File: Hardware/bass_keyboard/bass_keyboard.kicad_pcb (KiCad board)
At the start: 2 copper layers, 291.3 x 154.8 mm, 188 parts, among them J1 Conn_02x17_Top_Bottom

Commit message: Redo traces on bass keyboard
Completely started over on the traces, decided that the automatic routing was whack. Much happier with the new layout, increased orderliness and legibility, less prone to manufacturing error due to via clearance. Also adjusted speaker connection to better fit 16 AWG speaker wire.
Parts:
- LS1: footprint Connector_Wire:SolderWire-2sqmm_1x02_P7.8mm_D2mm_OD3.9mm -> Connector_Wire:SolderWire-1sqmm_1x02_P5.4mm_D1.4mm_OD2.7mm
- moved D79 0.67 mm to (61.1, 206.5)
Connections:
- J1 pad 11: unconnected-(J1-Pin_11-Pad11) -> ROW6
- J1 pad 34: ROW6 -> unconnected-(J1-Pin_34-Pad34)
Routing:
- net (no net): track 110.5 -> 0.00 mm
- net ROW2: track 449.9 -> 376.0 mm, vias 2 -> 0
- net ROW0: track 488.0 -> 426.7 mm
- net ROW5: track 374.3 -> 316.5 mm, vias 4 -> 0
- net ROW3: track 411.6 -> 365.3 mm, vias 2 -> 0
- net ROW4: track 301.9 -> 338.9 mm, vias 4 -> 0
- net COL12: track 333.5 -> 369.8 mm
- net Net-(D95_Dom7-K): track 236.6 -> 257.5 mm
- net COL1: track 159.7 -> 179.4 mm
- net COL8: track 273.4 -> 290.1 mm, vias 2 -> 0
- net COL9: track 291.5 -> 307.8 mm, vias 2 -> 0
- net Net-(D93_Dim1-K): track 229.2 -> 245.0 mm
- net COL2: track 176.6 -> 192.2 mm
- net Net-(J1-Pin_19): track 331.0 -> 316.0 mm
- net COL11: track 337.6 -> 352.4 mm
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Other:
- board text added: "Synharmonium Bass Keyboard Protoyping Master rev 0.2"
- board text removed: "Synharmonium Bass Keyboard Protoyping Master rev 0.1"

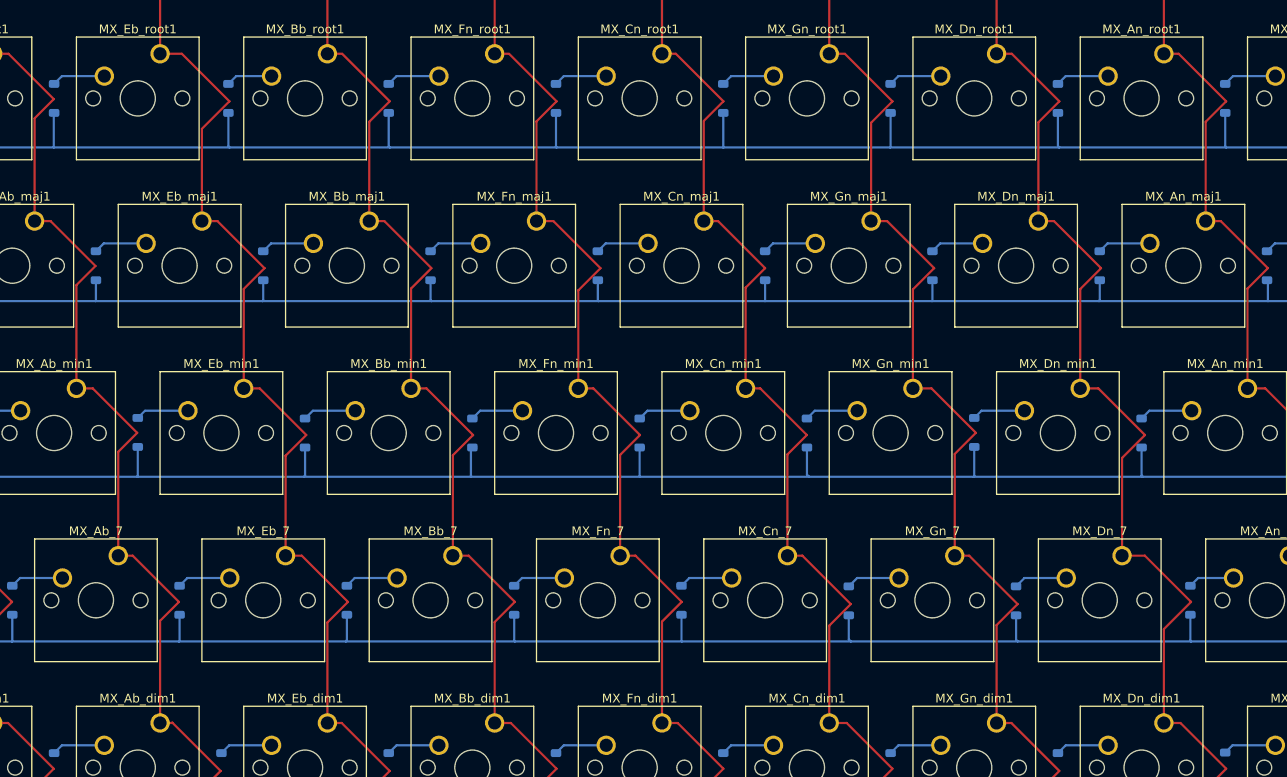
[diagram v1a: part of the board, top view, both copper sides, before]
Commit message: Added Website folder
A custom web page will be hosted through github, and the source files will be stored here.
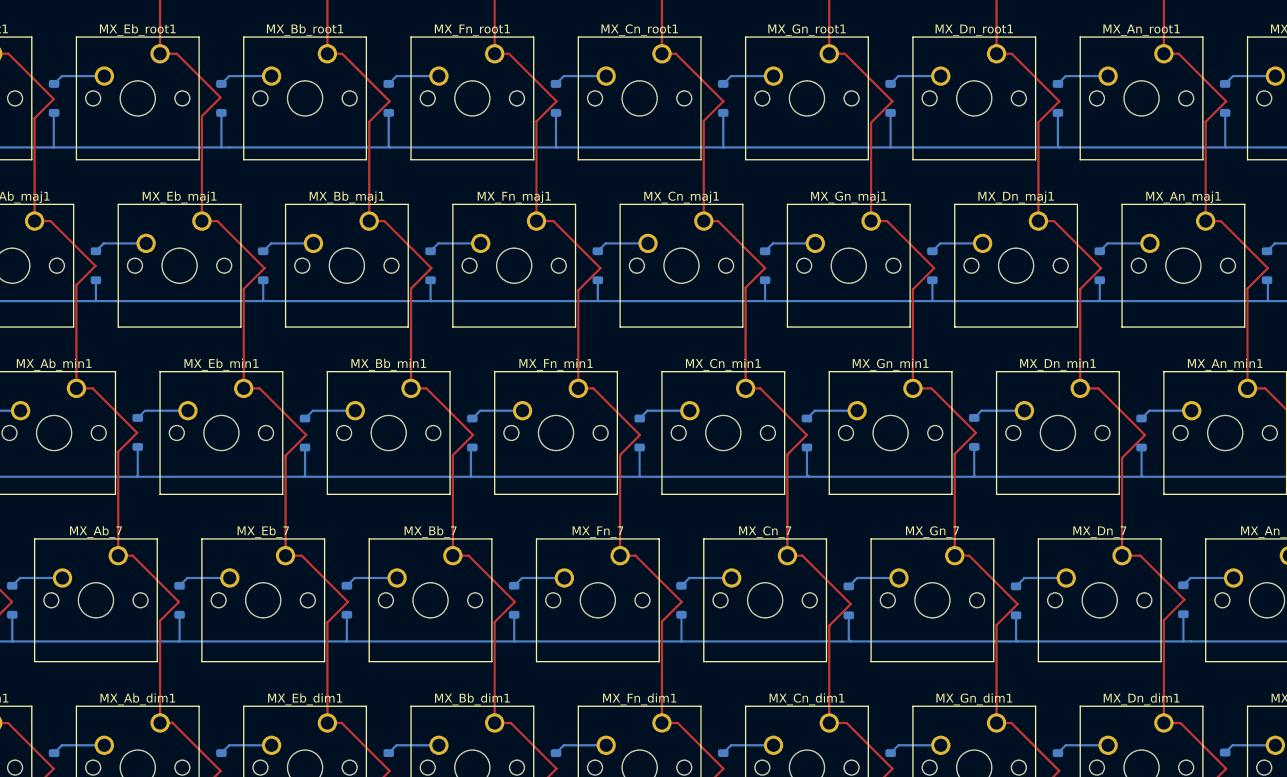
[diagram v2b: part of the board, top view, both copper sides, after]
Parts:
- moved D61 0.80 mm to (206.4, 169.0)
- moved D17 0.79 mm to (96.8, 111.9)
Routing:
- net COL2: track 192.2 -> 191.0 mm
- net COL7: track 275.2 -> 274.3 mm
- net Net-(D17-A): track 5.29 -> 6.08 mm
- net Net-(D61-A): track 5.29 -> 6.06 mm
